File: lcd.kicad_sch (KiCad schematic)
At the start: 9 parts, among them J2 FPC-05F-12PH20, Q1 SS8050

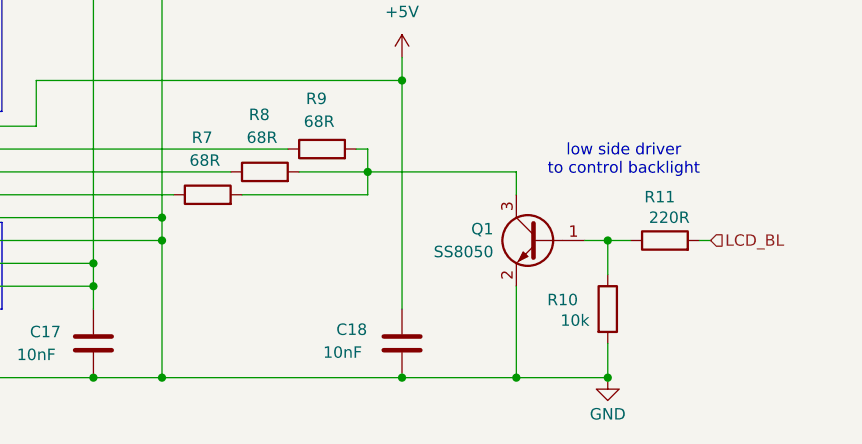
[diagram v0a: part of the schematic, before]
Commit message: fix usb and add esd diodes, some other checks
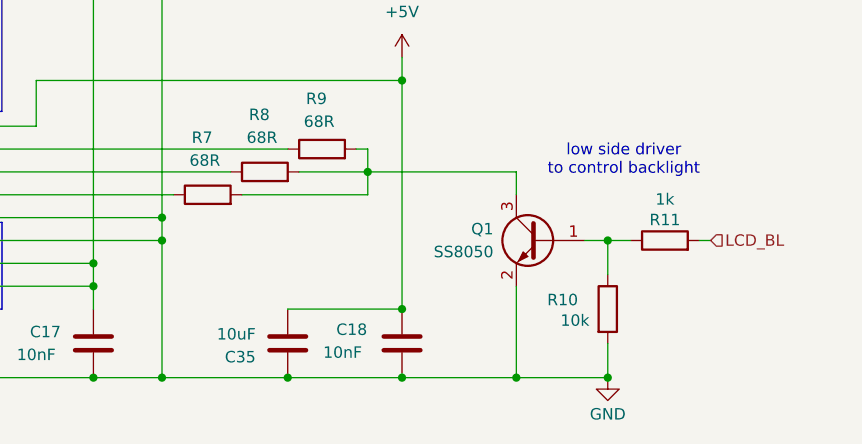
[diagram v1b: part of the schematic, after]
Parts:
- added C35: 10uF, Capacitor_SMD:C_0603_1608Metric, symbol Device:C
- R11: value 220R -> 1k; footprint Resistor_SMD:R_0603_1608Metric -> Resistor_SMD:R_0402_1005Metric
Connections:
- net +5V: now also C35.1
- net GND: now also C35.2
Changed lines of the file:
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@@
+	)
+	(junction
+		(at 121.92 161.29)
+		(diameter 0)
+		(color 0 0 0 0)
 	)
 	(junction
@@
 	)
 	(junction
+		(at 109.22 168.91)
+		(diameter 0)
+		(color 0 0 0 0)
+	)
+	(junction
 		(at 87.63 74.93)
 		(diameter 0)
@@
 	(wire
 		(pts
+			(xy 109.22 161.29) (xy 121.92 161.29)
+		)
+		(stroke
+			(width 0)
+			(type default)
+		)
+	)
+	(wire
+		(pts
 			(xy 121.92 133.35) (xy 121.92 135.89)
 		)
@@
 	(wire
 		(pts
-			(xy 95.25 168.91) (xy 121.92 168.91)
+			(xy 95.25 168.91) (xy 109.22 168.91)
 		)
 		(stroke
@@
 		(pts
 			(xy 74.93 158.75) (xy 87.63 158.75)
+		)
+		(stroke
+			(width 0)
+			(type default)
+		)
+	)
+	(wire
+		(pts
+			(xy 109.22 168.91) (xy 121.92 168.91)
 		)
 		(stroke
@@
 			)
 			(justify left)
+		)
+	)
+	(symbol
+		(lib_id "Device:C")
+		(at 109.22 165.1 0)
+		(unit 1)
+		(exclude_from_sim no)
+		(in_bom yes)
+		(on_board yes)
+		(dnp no)
+		(property "Reference" "C35"
+			(at 105.664 166.624 0)
+			(effects
+				(font
+					(size 1.27 1.27)
+				)
+				(justify right)
+			)
+		)
+		(property "Value" "10uF"
+			(at 105.664 164.084 0)
+			(effects
+				(font
+					(size 1.27 1.27)
+				)
+				(justify right)
+			)
+		)
+		(property "Footprint" "Capacitor_SMD:C_0603_1608Metric"
+			(at 110.1852 168.91 0)
+			(effects
+				(font
+					(size 1.27 1.27)
+				)
+				(hide yes)
+			)
+		)
+		(property "Datasheet" "~"
+			(at 109.22 165.1 0)
+			(effects
+				(font
+					(size 1.27 1.27)
+				)
+				(hide yes)
+			)
+		)
+		(property "Description" "Unpolarized capacitor"
+			(at 109.22 165.1 0)
+			(effects
+				(font
+					(size 1.27 1.27)
+				)
+				(hide yes)
+			)
+		)
+		(property "LCSC" ""
+			(at 109.22 165.1 0)
+			(effects
+				(font
+					(size 1.27 1.27)
+				)
+				(hide yes)
+			)
+		)
+		(property "Manufacturer" ""
+			(at 109.22 165.1 0)
+			(effects
+				(font
+					(size 1.27 1.27)
+				)
+				(hide yes)
+			)
+		)
+		(property "Manufacturer Part Number" ""
+			(at 109.22 165.1 0)
+			(effects
+				(font
+					(size 1.27 1.27)
+				)
+				(hide yes)
+			)
+		)
+		(pin "2"
+		)
+		(pin "1"
+		)
+		(instances
+			(project "gameboy"
+				(path "/f4643692-c319-40a7-82a2-3e775c0a417f/d0993c89-522c-4206-a2f2-b5b66c7e7b73"
+					(reference "C35")
+					(unit 1)
+				)
+			)
 		)
 	)
@@
 		(dnp no)
 		(fields_autoplaced yes)
-		(property "Reference" "#PWR033"
+		(property "Reference" "#PWR019"
 			(at 121.92 137.16 0)
 			(effects
@@
 			(project "gameboy"
 				(path "/f4643692-c319-40a7-82a2-3e775c0a417f/d0993c89-522c-4206-a2f2-b5b66c7e7b73"
-					(reference "#PWR033")
+					(reference "#PWR019")
 					(unit 1)
 				)
@@
 				(path "/f4643692-c319-40a7-82a2-3e775c0a417f/d0993c89-522c-4206-a2f2-b5b66c7e7b73"
 					(reference "R10")
+					(unit 1)
+				)
+			)
+		)
+	)
+	(symbol
+		(lib_id "Device:R")
+		(at 151.13 153.67 90)
+		(unit 1)
+		(exclude_from_sim no)
+		(in_bom yes)
+		(on_board yes)
+		(dnp no)
+		(property "Reference" "R11"
+			(at 151.13 151.384 90)
+			(effects
+				(font
+					(size 1.27 1.27)
+				)
+			)
+		)
+		(property "Value" "1k"
+			(at 151.13 149.098 90)
+			(effects
+				(font
+					(size 1.27 1.27)
+				)
+			)
+		)
+		(property "Footprint" "Resistor_SMD:R_0402_1005Metric"
+			(at 151.13 155.448 90)
+			(effects
+				(font
+					(size 1.27 1.27)
+				)
+				(hide yes)
+			)
+		)
+		(property "Datasheet" "~"
+			(at 151.13 153.67 0)
+			(effects
+				(font
+					(size 1.27 1.27)
+				)
+				(hide yes)
+			)
+		)
+		(property "Description" ""
+			(at 151.13 153.67 0)
+			(effects
+				(font
+					(size 1.27 1.27)
+				)
+			)
+		)
+		(pin "1"
+		)
+		(pin "2"
+		)
+		(instances
+			(project "gameboy"
+				(path "/f4643692-c319-40a7-82a2-3e775c0a417f/d0993c89-522c-4206-a2f2-b5b66c7e7b73"
+					(reference "R11")
 					(unit 1)
 				)
@@
 					(unit 1)
 				)
-			)
-		)
-	)
-	(symbol
-		(lib_id "Device:R")
-		(at 151.13 153.67 90)
-		(unit 1)
-		(exclude_from_sim no)
-		(in_bom yes)
-		(on_board yes)
-		(dnp no)
-		(property "Reference" "R11"
-			(at 148.844 148.844 90)
-			(effects
-				(font
-					(size 1.27 1.27)
-				)
-				(justify right)
-			)
-		)
-		(property "Value" "220R"
-			(at 149.352 151.13 90)
-			(effects
-				(font
-					(size 1.27 1.27)
-				)
-				(justify right)
-			)
-		)
-		(property "Footprint" "Resistor_SMD:R_0603_1608Metric"
-			(at 151.13 155.448 90)
-			(effects
-				(font
-					(size 1.27 1.27)
-				)
-				(hide yes)
-			)
-		)
-		(property "Datasheet" "~"
-			(at 151.13 153.67 0)
-			(effects
-				(font
-					(size 1.27 1.27)
-				)
-				(hide yes)
-			)
-		)
-		(property "Description" "Resistor"
-			(at 151.13 153.67 0)
-			(effects
-				(font
-					(size 1.27 1.27)
-				)
-				(hide yes)
-			)
-		)
-		(property "LCSC" ""
-			(at 151.13 153.67 0)
-			(effects
-				(font
-					(size 1.27 1.27)
-				)
-				(hide yes)
-			)
-		)
-		(property "Manufacturer" ""
-			(at 151.13 153.67 0)
-			(effects
-				(font
-					(size 1.27 1.27)
-				)
-				(hide yes)
-			)
-		)
-		(property "Manufacturer Part Number" ""
-			(at 151.13 153.67 0)
-			(effects
-				(font
-					(size 1.27 1.27)
-				)
-				(hide yes)
-			)
-		)
-		(pin "1"
-		)
-		(pin "2"
-		)
-		(instances
-			(project "gameboy"
-				(path "/f4643692-c319-40a7-82a2-3e775c0a417f/d0993c89-522c-4206-a2f2-b5b66c7e7b73"
-					(reference "R11")
-					(unit 1)
-				)

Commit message: whole bunch of layout done
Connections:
- net +5V renamed VDC
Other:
- note added: "check resistors backlight over voltage range 3.7-3.3"
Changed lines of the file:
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@@
+		)
+	)
+	(text "check resistors backlight\nover voltage range 3.7-3.3"
+		(exclude_from_sim no)
+		(at 111.76 122.936 0)
+		(effects
+			(font
+				(size 1.27 1.27)
+			)
 		)
 	)
@@
 	)
 	(symbol
-		(lib_id "power:+5V")
-		(at 121.92 133.35 0)
-		(unit 1)
-		(exclude_from_sim no)
-		(in_bom yes)
-		(on_board yes)
-		(dnp no)
-		(fields_autoplaced yes)
-		(property "Reference" "#PWR019"
-			(at 121.92 137.16 0)
-			(effects
-				(font
-					(size 1.27 1.27)
-				)
-				(hide yes)
-			)
-		)
-		(property "Value" "+5V"
-			(at 121.92 128.27 0)
-			(effects
-				(font
-					(size 1.27 1.27)
-				)
-			)
-		)
-		(property "Footprint" ""
-			(at 121.92 133.35 0)
-			(effects
-				(font
-					(size 1.27 1.27)
-				)
-				(hide yes)
-			)
-		)
-		(property "Datasheet" ""
-			(at 121.92 133.35 0)
-			(effects
-				(font
-					(size 1.27 1.27)
-				)
-				(hide yes)
-			)
-		)
-		(property "Description" "Power symbol creates a global label with name \"+5V\""
-			(at 121.92 133.35 0)
-			(effects
-				(font
-					(size 1.27 1.27)
-				)
-				(hide yes)
-			)
-		)
-		(pin "1"
-		)
-		(instances
-			(project "gameboy"
-				(path "/f4643692-c319-40a7-82a2-3e775c0a417f/d0993c89-522c-4206-a2f2-b5b66c7e7b73"
-					(reference "#PWR019")
-					(unit 1)
-				)
-			)
-		)
-	)
-	(symbol
 		(lib_id "power:GND")
 		(at 144.78 168.91 0)
@@
 					(unit 1)
 				)
+			)
+		)
+	)
+	(symbol
+		(lib_id "power:VDC")
+		(at 121.92 133.35 0)
+		(unit 1)
+		(exclude_from_sim no)
+		(in_bom yes)
+		(on_board yes)
+		(dnp no)
+		(fields_autoplaced yes)
+		(property "Reference" "#PWR019"
+			(at 121.92 137.16 0)
+			(effects
+				(font
+					(size 1.27 1.27)
+				)
+				(hide yes)
+			)
+		)
+		(property "Value" "VDC"
+			(at 121.92 128.27 0)
+			(effects
+				(font
+					(size 1.27 1.27)
+				)
+			)
+		)
+		(property "Footprint" ""
+			(at 121.92 133.35 0)
+			(effects
+				(font
+					(size 1.27 1.27)
+				)
+				(hide yes)
+			)
+		)
+		(property "Datasheet" ""
+			(at 121.92 133.35 0)
+			(effects
+				(font
+					(size 1.27 1.27)
+				)
+				(hide yes)
+			)
+		)
+		(property "Description" "Power symbol creates a global label with name \"VDC\""
+			(at 121.92 133.35 0)
+			(effects
+				(font
+					(size 1.27 1.27)
+				)
+				(hide yes)
+			)
+		)
+		(pin "1"
+		)
+		(instances
+			(project ""
+				(path "/f4643692-c319-40a7-82a2-3e775c0a417f/d0993c89-522c-4206-a2f2-b5b66c7e7b73"
+					(reference "#PWR019")
+					(unit 1)
+				)

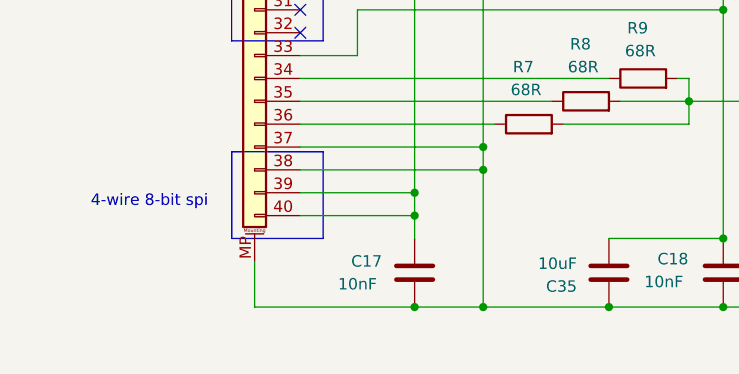
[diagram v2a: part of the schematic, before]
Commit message: overhaul mcu layout, add last components, stitching vias, run DRC
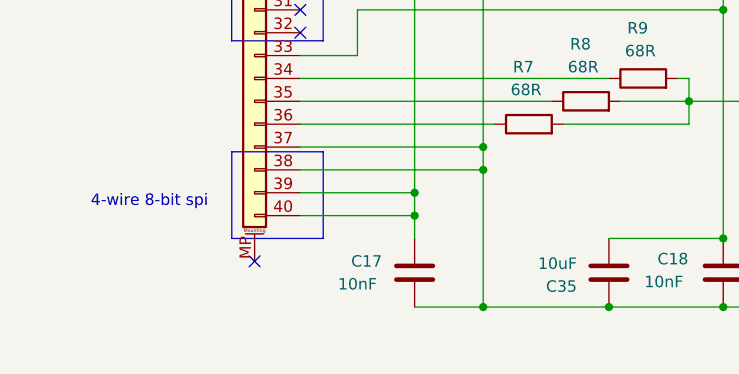
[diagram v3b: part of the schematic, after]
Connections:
- net GND: no longer J2.MP (MountPin)
- no-connect marks 22 -> 23
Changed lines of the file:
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@@
-	)
-	(junction
-		(at 87.63 168.91)
-		(diameter 0)
-		(color 0 0 0 0)
 	)
 	(junction
@@
 	)
 	(no_connect
+		(at 69.85 163.83)
+	)
+	(no_connect
 		(at 74.93 138.43)
 	)
@@
 	(wire
 		(pts
-			(xy 69.85 168.91) (xy 87.63 168.91)
-		)
-		(stroke
-			(width 0)
-			(type default)
-		)
-	)
-	(wire
-		(pts
 			(xy 74.93 151.13) (xy 95.25 151.13)
 		)
@@
 		)
 		(stroke
-			(width 0)
-			(type default)
-		)
-	)
-	(wire
-		(pts
-			(xy 69.85 163.83) (xy 69.85 168.91)
-		)
-		(stroke

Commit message: add silkscreen, optimize layout and replace sd card peripheral
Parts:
- added TP8: TestPoint, TestPoint:TestPoint_Pad_D1.0mm, symbol Connector:TestPoint
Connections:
- net LCD_BL: now also TP8.1
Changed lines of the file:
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@@
+	)
+	(junction
+		(at 162.56 153.67)
+		(diameter 0)
+		(color 0 0 0 0)
 	)
 	(junction
@@
 	(wire
 		(pts
-			(xy 154.94 153.67) (xy 156.21 153.67)
+			(xy 154.94 153.67) (xy 162.56 153.67)
 		)
 		(stroke
@@
 	(wire
 		(pts
-			(xy 134.62 146.05) (xy 118.11 146.05)
-		)
-		(stroke
-			(width 0)
-			(type default)
-		)
-	)
-	(wire
-		(pts
 			(xy 74.93 156.21) (xy 87.63 156.21)
 		)
@@
 	(wire
 		(pts
+			(xy 118.11 146.05) (xy 134.62 146.05)
+		)
+		(stroke
+			(width 0)
+			(type default)
+		)
+	)
+	(wire
+		(pts
 			(xy 104.14 148.59) (xy 118.11 148.59)
 		)
@@
 		(pts
 			(xy 118.11 146.05) (xy 110.49 146.05)
+		)
+		(stroke
+			(width 0)
+			(type default)
+		)
+	)
+	(wire
+		(pts
+			(xy 162.56 153.67) (xy 171.45 153.67)
 		)
 		(stroke
@@
 	(hierarchical_label "LCD_BL"
 		(shape input)
-		(at 156.21 153.67 0)
+		(at 171.45 153.67 0)
 		(effects
 			(font
@@
 					(unit 1)
 				)
+			)
+		)
+	)
+	(symbol
+		(lib_id "Connector:TestPoint")
+		(at 162.56 153.67 0)
+		(unit 1)
+		(exclude_from_sim no)
+		(in_bom yes)
+		(on_board yes)
+		(dnp no)
+		(property "Reference" "TP8"
+			(at 158.75 145.034 0)
+			(effects
+				(font
+					(size 1.27 1.27)
+				)
+				(justify left)
+			)
+		)
+		(property "Value" "TestPoint"
+			(at 158.75 147.574 0)
+			(effects
+				(font
+					(size 1.27 1.27)
+				)
+				(justify left)
+			)
+		)
+		(property "Footprint" "TestPoint:TestPoint_Pad_D1.0mm"
+			(at 167.64 153.67 0)
+			(effects
+				(font
+					(size 1.27 1.27)
+				)
+				(hide yes)
+			)
+		)
+		(property "Datasheet" "~"
+			(at 167.64 153.67 0)
+			(effects
+				(font
+					(size 1.27 1.27)
+				)
+				(hide yes)
+			)
+		)
+		(property "Description" "test point"
+			(at 162.56 153.67 0)
+			(effects
+				(font
+					(size 1.27 1.27)
+				)
+				(hide yes)
+			)
+		)
+		(property "LCSC" ""
+			(at 162.56 153.67 0)
+			(effects
+				(font
+					(size 1.27 1.27)
+				)
+				(hide yes)
+			)
+		)
+		(property "Manufacturer" ""
+			(at 162.56 153.67 0)
+			(effects
+				(font
+					(size 1.27 1.27)
+				)
+				(hide yes)
+			)
+		)
+		(property "Manufacturer Part Number" ""
+			(at 162.56 153.67 0)
+			(effects
+				(font
+					(size 1.27 1.27)
+				)
+				(hide yes)
+			)
+		)
+		(pin "1"
+		)
+		(instances
+			(project "gameboy"
+				(path "/f4643692-c319-40a7-82a2-3e775c0a417f/d0993c89-522c-4206-a2f2-b5b66c7e7b73"
+					(reference "TP8")
+					(unit 1)
+				)
